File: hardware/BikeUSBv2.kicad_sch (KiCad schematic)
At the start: 51 parts, among them J1 TYPE-C-31-M-16, J2 JST S2B-EH(LF)(SN), SW1 1TS002E-2500-2501-CT, SW2 1TS002E-2500-2501-CT, U1 TPS63070, U2 ATtiny1616-M, U3 FUSB302B10MPX, U4 HT7550

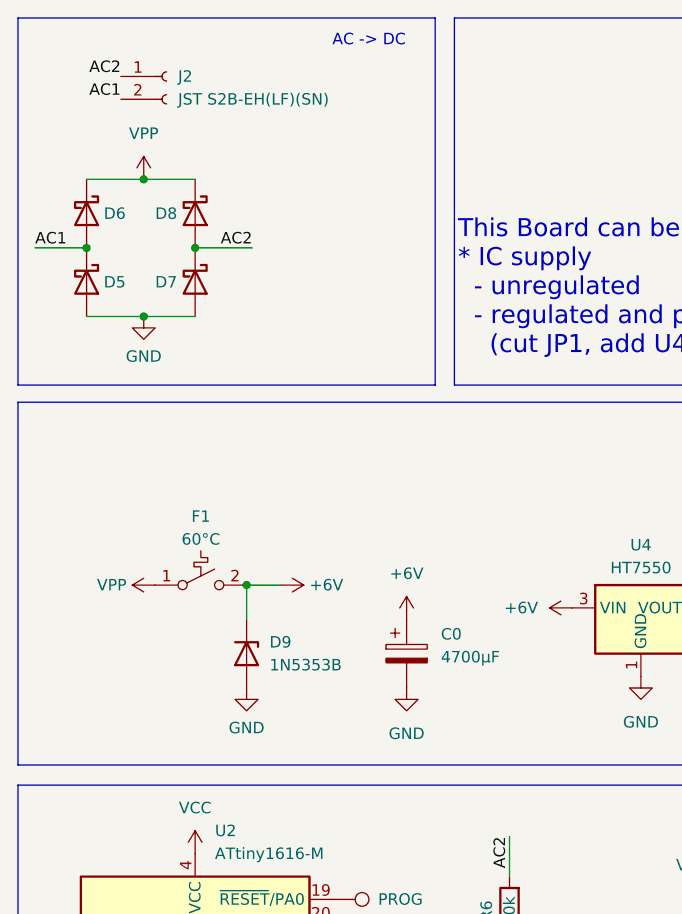
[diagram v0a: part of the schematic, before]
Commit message: [PCB] switch to different protection circuit
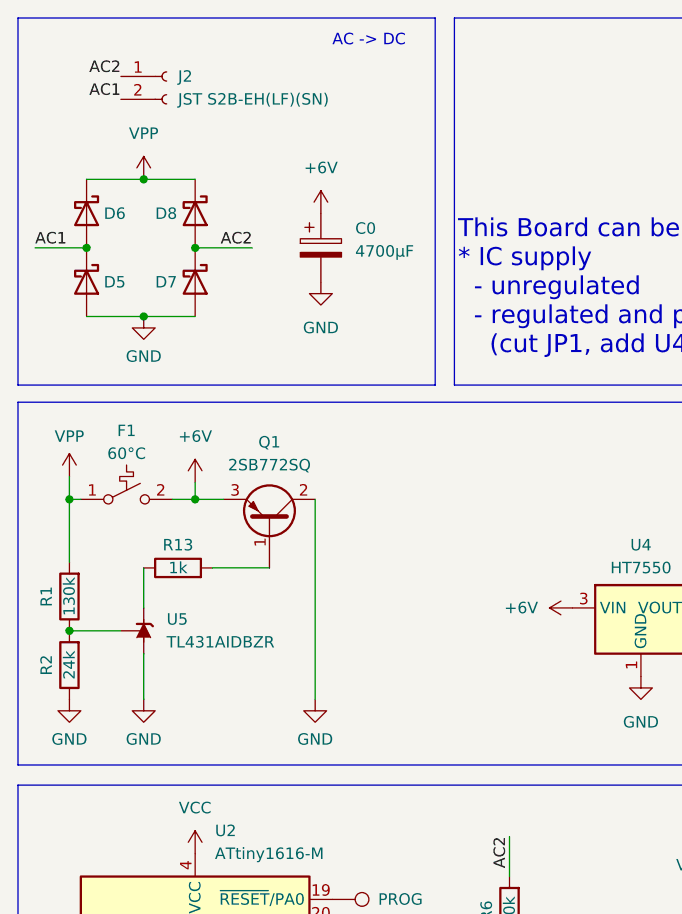
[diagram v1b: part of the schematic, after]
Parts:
- removed D9: 1N5353B, Diode_THT:D_DO-15_P5.08mm_Vertical_KathodeUp, symbol Device:D_Zener
- added Q1: 2SB772SQ, Package_TO_SOT_SMD:SOT-89-3_Handsoldering, symbol Device:Q_PNP_BCE
- added R1: 130k, Resistor_SMD:R_0805_2012Metric_Pad1.20x1.40mm_HandSolder, symbol Device:R
- added R13: 1k, Resistor_SMD:R_0805_2012Metric_Pad1.20x1.40mm_HandSolder, symbol Device:R
- added R2: 24k, Resistor_SMD:R_0805_2012Metric_Pad1.20x1.40mm_HandSolder, symbol Device:R
- added U5: TL431AIDBZR, Package_TO_SOT_SMD:SOT-23_Handsoldering, symbol Reference_Voltage:TL431DBZ
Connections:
- net +6V: now also Q1.3 (E)
- net GND: now also Q1.2 (C), R2.1, U5.3 (A)
- net VPP: now also R1.2
- new net: R13.1, U5.1 (K)
- new net: Q1.1 (B), R13.2
- new net: R1.1, R2.2, U5.2 (REF)
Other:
- moved on the sheet: C0, F1

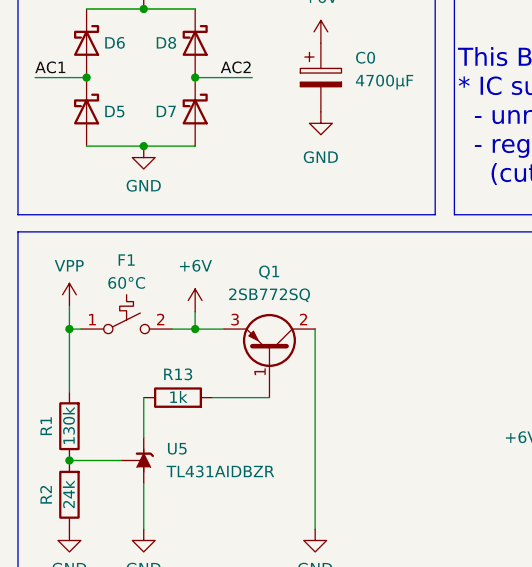
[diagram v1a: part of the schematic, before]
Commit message: [PCB] fill in LCSC IDs
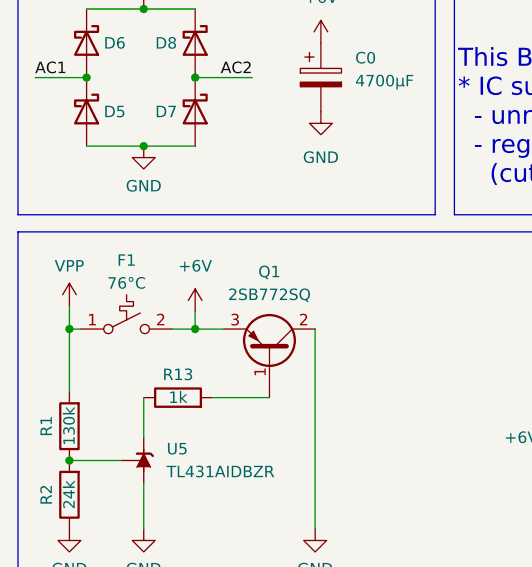
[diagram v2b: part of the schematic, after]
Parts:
- F1: value 60°C -> 76°C; LCSC (none) -> C22396315; Manufacturer (none) -> SETsafe | SETfuse; Part # (none) -> X0
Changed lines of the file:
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@@
       (effects (font (size 1.27 1.27)))
     )
-    (property "Value" "60°C" (at 28.575 65.405 0)
+    (property "Value" "76°C" (at 28.575 65.405 0)
       (effects (font (size 1.27 1.27)))
     )
@@
       (effects (font (size 1.27 1.27)) hide)
     )
+    (property "LCSC" "C22396315" (at 28.575 70.485 0)
+      (effects (font (size 1.27 1.27)) hide)
+    )
+    (property "Part #" "X0" (at 28.575 70.485 0)
+      (effects (font (size 1.27 1.27)) hide)
+    )
+    (property "Manufacturer" "SETsafe | SETfuse" (at 28.575 70.485 0)
+      (effects (font (size 1.27 1.27)) hide)
+    )

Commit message: idk
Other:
- moved on the sheet: D1, R8, U4

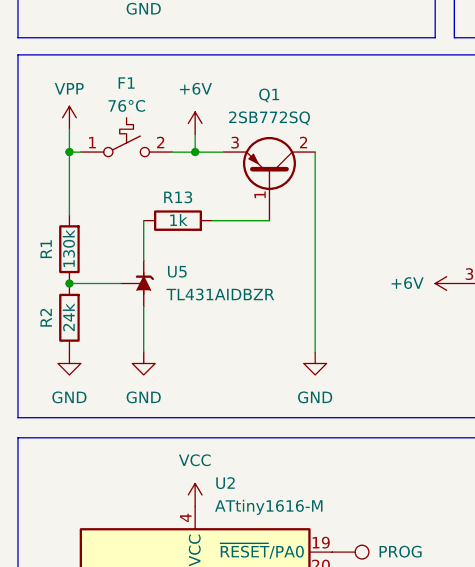
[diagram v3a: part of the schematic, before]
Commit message: [PCB] changed VREG RDIV for more accurate 5V
prev 5.13V now 4.98V
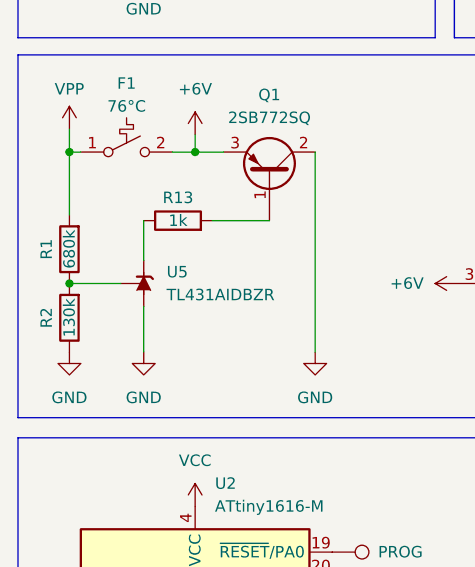
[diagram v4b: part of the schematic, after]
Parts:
- R1: value 130k -> 680k; LCSC C110774 -> (none)
- R2: value 24k -> 130k; LCSC C110774 -> (none)
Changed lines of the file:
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@@
       (effects (font (size 1.27 1.27)))
     )
-    (property "Value" "130k" (at 22.225 81.28 90)
+    (property "Value" "680k" (at 22.225 81.28 90)
       (effects (font (size 1.27 1.27)))
     )
@@
     )
     (property "Datasheet" "~" (at 22.225 81.28 0)
-      (effects (font (size 1.27 1.27)) hide)
-    )
-    (property "LCSC" "C110774" (at 19.685 81.28 0)
       (effects (font (size 1.27 1.27)) hide)
     )
@@
       (effects (font (size 1.27 1.27)))
     )
-    (property "Value" "24k" (at 22.225 88.9 90)
+    (property "Value" "130k" (at 22.225 88.9 90)
       (effects (font (size 1.27 1.27)))
     )
@@
       (effects (font (size 1.27 1.27)) hide)
     )
-    (property "LCSC" "C110774" (at 19.685 88.9 0)
-      (effects (font (size 1.27 1.27)) hide)
-    )

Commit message: [PCB] slight sch change
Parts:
- added R14: 10k, Resistor_SMD:R_0805_2012Metric_Pad1.20x1.40mm_HandSolder, symbol Device:R
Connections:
- net +6V: now also R1.2, R14.2
- net VPP: no longer R1.2
- net at R13.1, U5.1 (K): now also R14.1
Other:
- moved on the sheet: R13
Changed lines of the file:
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@@
   (junction (at 161.925 27.305) (diameter 0) (color 0 0 0 0)
   )
+  (junction (at 30.48 73.66) (diameter 0) (color 0 0 0 0)
+  )
   (junction (at 142.24 57.15) (diameter 0) (color 0 0 0 0)
   )
@@
   (junction (at 151.765 27.305) (diameter 0) (color 0 0 0 0)
   )
+  (junction (at 30.48 81.28) (diameter 0) (color 0 0 0 0)
+  )
   (junction (at 71.12 120.015) (diameter 0) (color 0 0 0 0)
   )
@@
   (junction (at 151.765 34.925) (diameter 0) (color 0 0 0 0)
   )
-  (junction (at 22.225 70.485) (diameter 0) (color 0 0 0 0)
-  )
   (junction (at 142.24 27.305) (diameter 0) (color 0 0 0 0)
   )
@@
     (stroke (width 0) (type default))
   )
+  (wire (pts (xy 36.195 70.485) (xy 36.195 73.66))
+    (stroke (width 0) (type default))
+  )
   (wire (pts (xy 156.21 127) (xy 160.655 127))
     (stroke (width 0) (type default))
@@
     (stroke (width 0) (type default))
   )
-  (wire (pts (xy 51.435 137.795) (xy 56.515 137.795))
+  (wire (pts (xy 44.45 81.28) (xy 44.45 78.105))
     (stroke (width 0) (type default))
   )
-  (wire (pts (xy 30.48 82.55) (xy 30.48 78.105))
+  (wire (pts (xy 51.435 137.795) (xy 56.515 137.795))
     (stroke (width 0) (type default))
   )
@@
     (stroke (width 0) (type default))
   )
+  (wire (pts (xy 30.48 81.28) (xy 30.48 82.55))
+    (stroke (width 0) (type default))
+  )
   (wire (pts (xy 146.05 114.3) (xy 156.21 114.3))
     (stroke (width 0) (type default))
@@
     (stroke (width 0) (type default))
   )
+  (wire (pts (xy 22.225 77.47) (xy 22.225 73.66))
+    (stroke (width 0) (type default))
+  )
   (wire (pts (xy 89.535 150.495) (xy 92.71 150.495))
     (stroke (width 0) (type default))
@@
     (stroke (width 0) (type default))
   )
-  (wire (pts (xy 22.225 70.485) (xy 22.225 77.47))
+  (wire (pts (xy 36.83 81.28) (xy 30.48 81.28))
     (stroke (width 0) (type default))
   )
@@
     (stroke (width 0) (type default))
   )
+  (wire (pts (xy 30.48 73.66) (xy 36.195 73.66))
+    (stroke (width 0) (type default))
+  )
   (wire (pts (xy 154.305 71.12) (xy 158.115 71.12))
     (stroke (width 0) (type default))
@@
     (stroke (width 0) (type default))
   )
+  (wire (pts (xy 22.225 73.66) (xy 30.48 73.66))
+    (stroke (width 0) (type default))
+  )
   (wire (pts (xy 156.21 83.82) (xy 158.115 83.82))
     (stroke (width 0) (type default))
@@
     (stroke (width 0) (type default))
   )
-  (wire (pts (xy 38.1 78.105) (xy 44.45 78.105))
-    (stroke (width 0) (type default))
-  )
   (wire (pts (xy 24.13 34.925) (xy 30.48 34.925))
     (stroke (width 0) (type default))
@@
     )
   )
-  (symbol (lib_id "Device:R") (at 34.29 78.105 90) (unit 1)
+  (symbol (lib_id "Device:R") (at 40.64 81.28 90) (unit 1)
     (in_bom yes) (on_board yes) (dnp no)
-    (property "Reference" "R13" (at 34.29 75.565 90)
+    (property "Reference" "R13" (at 40.64 78.74 90)
       (effects (font (size 1.27 1.27)))
     )
-    (property "Value" "1k" (at 34.29 78.105 90)
+    (property "Value" "1k" (at 40.64 81.28 90)
       (effects (font (size 1.27 1.27)))
     )
-    (property "Footprint" "Resistor_SMD:R_0805_2012Metric_Pad1.20x1.40mm_HandSolder" (at 34.29 79.883 90)
+    (property "Footprint" "Resistor_SMD:R_0805_2012Metric_Pad1.20x1.40mm_HandSolder" (at 40.64 83.058 90)
       (effects (font (size 1.27 1.27)) hide)
     )
-    (property "Datasheet" "~" (at 34.29 78.105 0)
+    (property "Datasheet" "~" (at 40.64 81.28 0)
       (effects (font (size 1.27 1.27)) hide)
     )
-    (property "LCSC" "C110774" (at 34.29 75.565 0)
+    (property "LCSC" "C110774" (at 40.64 78.74 0)
       (effects (font (size 1.27 1.27)) hide)
     )
@@
         )
       )
+    )
+  )
+  (symbol (lib_id "Device:R") (at 30.48 77.47 180) (unit 1)
+    (in_bom yes) (on_board no) (dnp yes)
+    (property "Reference" "R14" (at 27.94 77.47 90)
+      (effects (font (size 1.27 1.27)))
+    )
+    (property "Value" "10k" (at 30.48 77.47 90)
+      (effects (font (size 1.27 1.27)))
+    )
+    (property "Footprint" "Resistor_SMD:R_0805_2012Metric_Pad1.20x1.40mm_HandSolder" (at 32.258 77.47 90)
+      (effects (font (size 1.27 1.27)) hide)
+    )
+    (property "Datasheet" "~" (at 30.48 77.47 0)
+      (effects (font (size 1.27 1.27)) hide)
+    )
+    (property "LCSC" "C217770" (at 27.94 77.47 0)
+      (effects (font (size 1.27 1.27)) hide)
+    )
+    (property "Sim.Enable" "0" (at 30.48 77.47 0)
+      (effects (font (size 1.27 1.27)) hide)
+    )
+    (pin "1")
+    (pin "2")
+    (instances
+      (project "BikeUSBv2"
+        (path "/b4aff538-5116-4944-9d24-c26a88d7dfe8"
+          (reference "R14") (unit 1)
+        )
+      )

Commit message: {PCB] geo reannotate
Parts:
- renumbered C9 to C11, C11 to C12, C12 to C13, C0 to C14, C13 to C5, C5 to C6, C6 to C7, C7 to C8, C8 to C9, JP2 to JP1, R3 to R1, R9 to R10, R10 to R12, R12 to R13, R4 to R2, R5 to R3, R6 to R4, R13 to R5, R1 to R6, R2 to R7, R7 to R8, R8 to R9, SW2 to SW1, SW1 to SW2

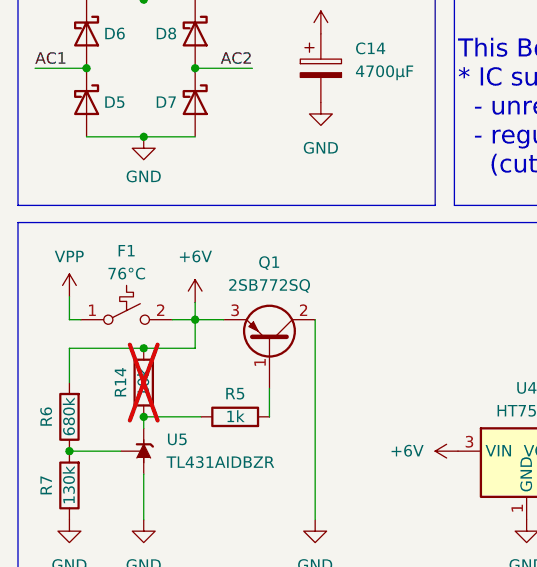
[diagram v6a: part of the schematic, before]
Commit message: [PCB] thermal fuse footprint now right pitch
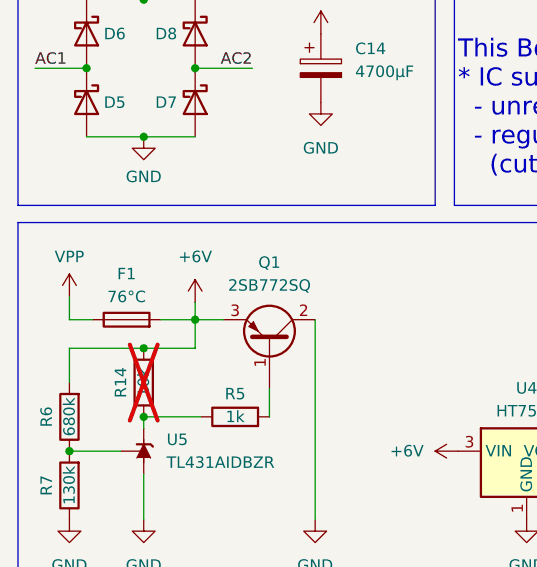
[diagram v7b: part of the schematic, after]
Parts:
- F1: footprint Connector_PinSocket_2.54mm:PinSocket_1x02_P2.54mm_Vertical -> H3_Other:SETfuse X-Series; symbol Switch:SW_SPST_Temperature -> Device:Fuse
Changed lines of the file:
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@@
     (stroke (width 0) (type default))
   )
-  (wire (pts (xy 22.225 70.485) (xy 23.495 70.485))
+  (wire (pts (xy 22.225 70.485) (xy 24.765 70.485))
     (stroke (width 0) (type default))
   )
@@
     (stroke (width 0) (type default))
   )
-  (wire (pts (xy 33.655 70.485) (xy 36.195 70.485))
+  (wire (pts (xy 32.385 70.485) (xy 36.195 70.485))
     (stroke (width 0) (type default))
   )
@@
     )
   )
-  (symbol (lib_id "Switch:SW_SPST_Temperature") (at 28.575 70.485 0) (unit 1)
-    (in_bom yes) (on_board yes) (dnp no)
-    (property "Reference" "F1" (at 28.575 62.865 0)
-      (effects (font (size 1.27 1.27)))
-    )
-    (property "Value" "76°C" (at 28.575 65.405 0)
-      (effects (font (size 1.27 1.27)))
-    )
-    (property "Footprint" "Connector_PinSocket_2.54mm:PinSocket_1x02_P2.54mm_Vertical" (at 28.575 70.485 0)
-      (effects (font (size 1.27 1.27)) hide)
-    )
+  (symbol (lib_id "Device:Fuse") (at 28.575 70.485 90) (unit 1)
+    (in_bom yes) (on_board yes) (dnp no)
+    (property "Reference" "F1" (at 28.575 65.405 90)
+      (effects (font (size 1.27 1.27)))
+    )
+    (property "Value" "76°C" (at 28.575 67.945 90)
+      (effects (font (size 1.27 1.27)))
+    )
+    (property "Footprint" "H3_Other:SETfuse X-Series" (at 28.575 70.485 0)
+      (effects (font (size 1.27 1.27)) hide)
+    )

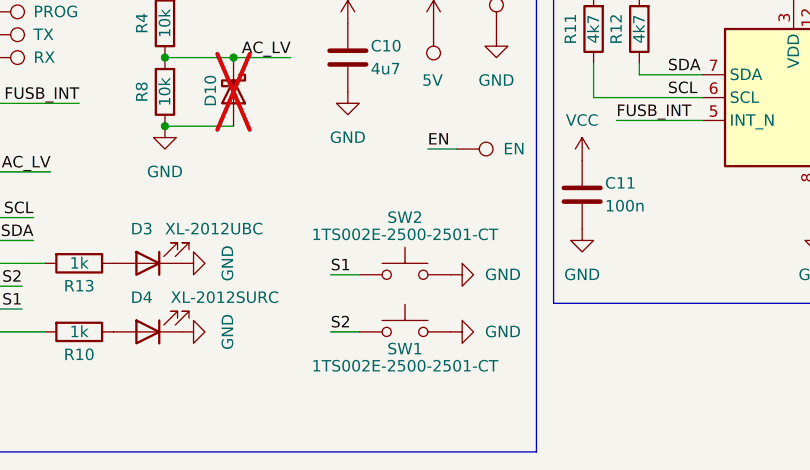
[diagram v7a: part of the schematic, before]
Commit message: [PCB] silkscreen fixes
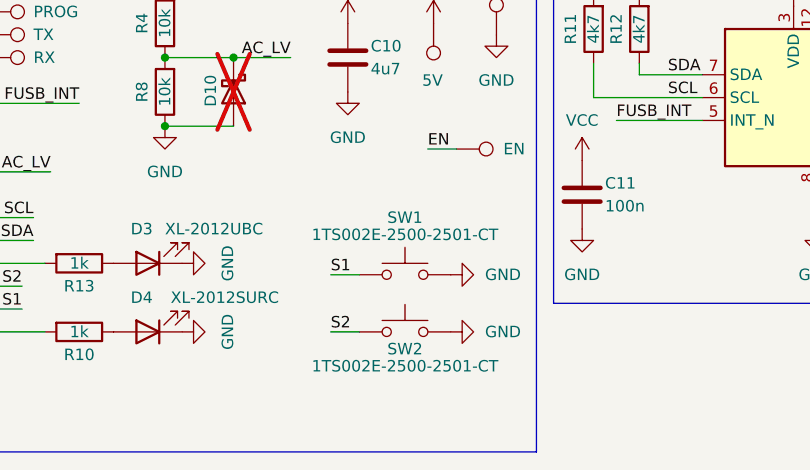
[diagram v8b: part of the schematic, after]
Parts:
- renumbered SW2 to SW1, SW1 to SW2
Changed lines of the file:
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@@
   (symbol (lib_id "Switch:SW_Push") (at 97.79 150.495 0) (unit 1)
     (in_bom yes) (on_board yes) (dnp no)
-    (property "Reference" "SW1" (at 97.79 152.4 0)
+    (property "Reference" "SW2" (at 97.79 152.4 0)
       (effects (font (size 1.27 1.27)))
     )
@@
       (project "BikeUSBv2"
         (path "/b4aff538-5116-4944-9d24-c26a88d7dfe8"
-          (reference "SW1") (unit 1)
+          (reference "SW2") (unit 1)
         )
       )
@@
   (symbol (lib_id "Switch:SW_Push") (at 97.79 144.145 0) (unit 1)
     (in_bom yes) (on_board yes) (dnp no)
-    (property "Reference" "SW2" (at 97.79 137.795 0)
+    (property "Reference" "SW1" (at 97.79 137.795 0)
       (effects (font (size 1.27 1.27)))
     )
@@
       (project "BikeUSBv2"
         (path "/b4aff538-5116-4944-9d24-c26a88d7dfe8"
-          (reference "SW2") (unit 1)
-        )
-      )
+          (reference "SW1") (unit 1)
+        )
+      )
